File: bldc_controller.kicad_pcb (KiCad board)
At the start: 4 copper layers, 99.1 x 99.1 mm, 151 parts, among them J1 Conn_01x06_Male, J2 Screw_Terminal_01x04, Q1 2N7002E, Q10 IRLB8721PBF, Q11 IRLB8721PBF, Q2 DMN65D8L-7, Q3 DMN65D8L-7, Q4 MMBT3904, Q5 IRF4905, Q6 IRLB8721PBF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

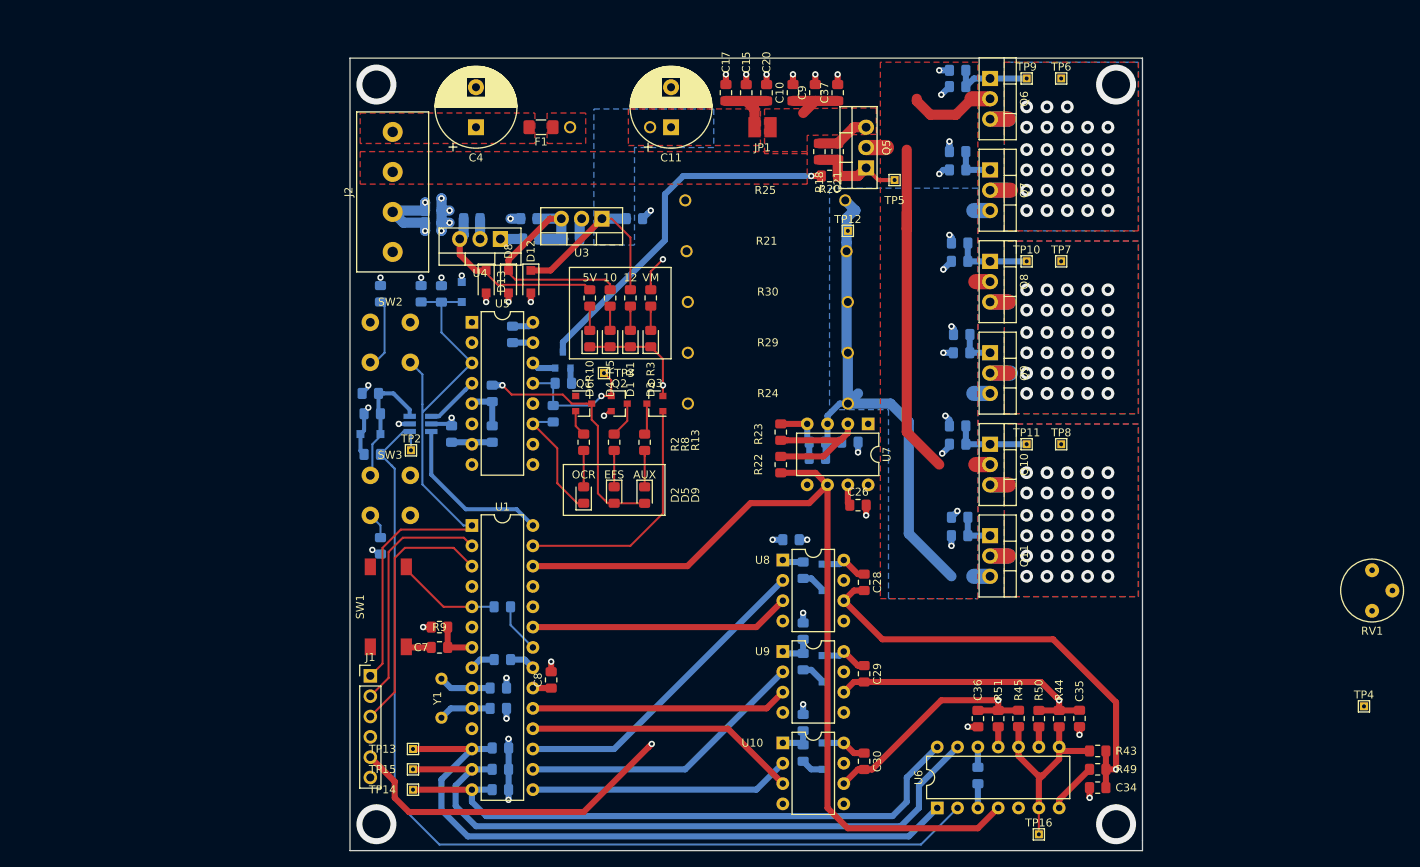
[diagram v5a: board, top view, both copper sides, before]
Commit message: Just Need to Fix Silkscreen
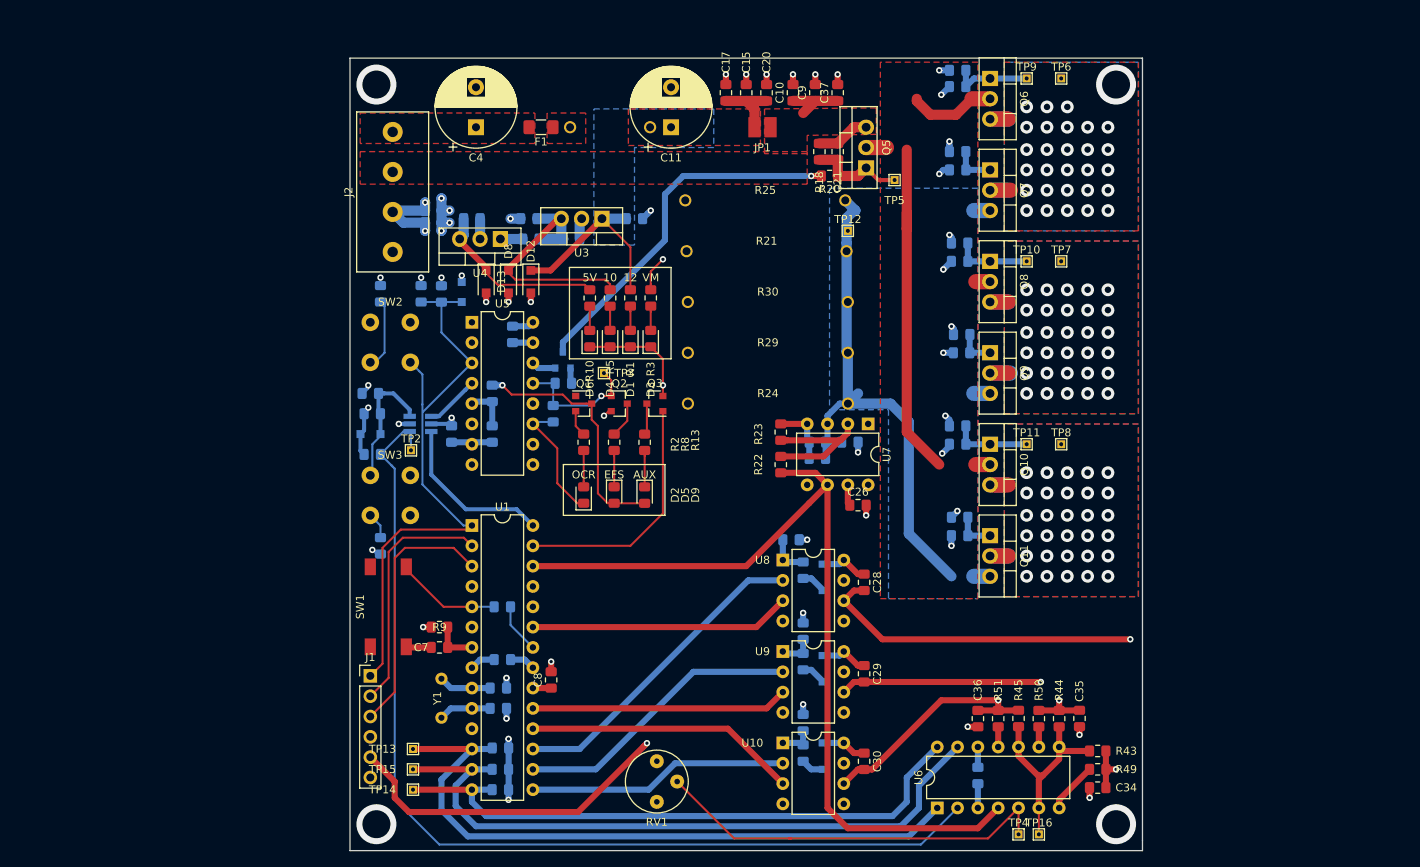
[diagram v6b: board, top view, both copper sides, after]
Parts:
- moved RV1 92.5 mm to (138.7, 129.8)
- moved TP4 46.0 mm to (183.9, 138.9)
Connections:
- RV1 pad 1: +5V -> GNDD
- RV1 pad 3: GNDD -> +5V
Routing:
- net Net-(RV1-Pad2): track 0.00 -> 50.8 mm
- net PhaseA: track 138.0 -> 128.1 mm, vias 29 -> 30
- net PhaseB: track 85.9 -> 82.7 mm, vias 31 -> 32
- net +5V: track 92.5 -> 91.8 mm
- net +12V: track 34.5 -> 33.8 mm
- net +10V: track 88.5 -> 88.6 mm, vias 2 -> 1

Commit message: Just Need to Fix Bottom Silkscreen
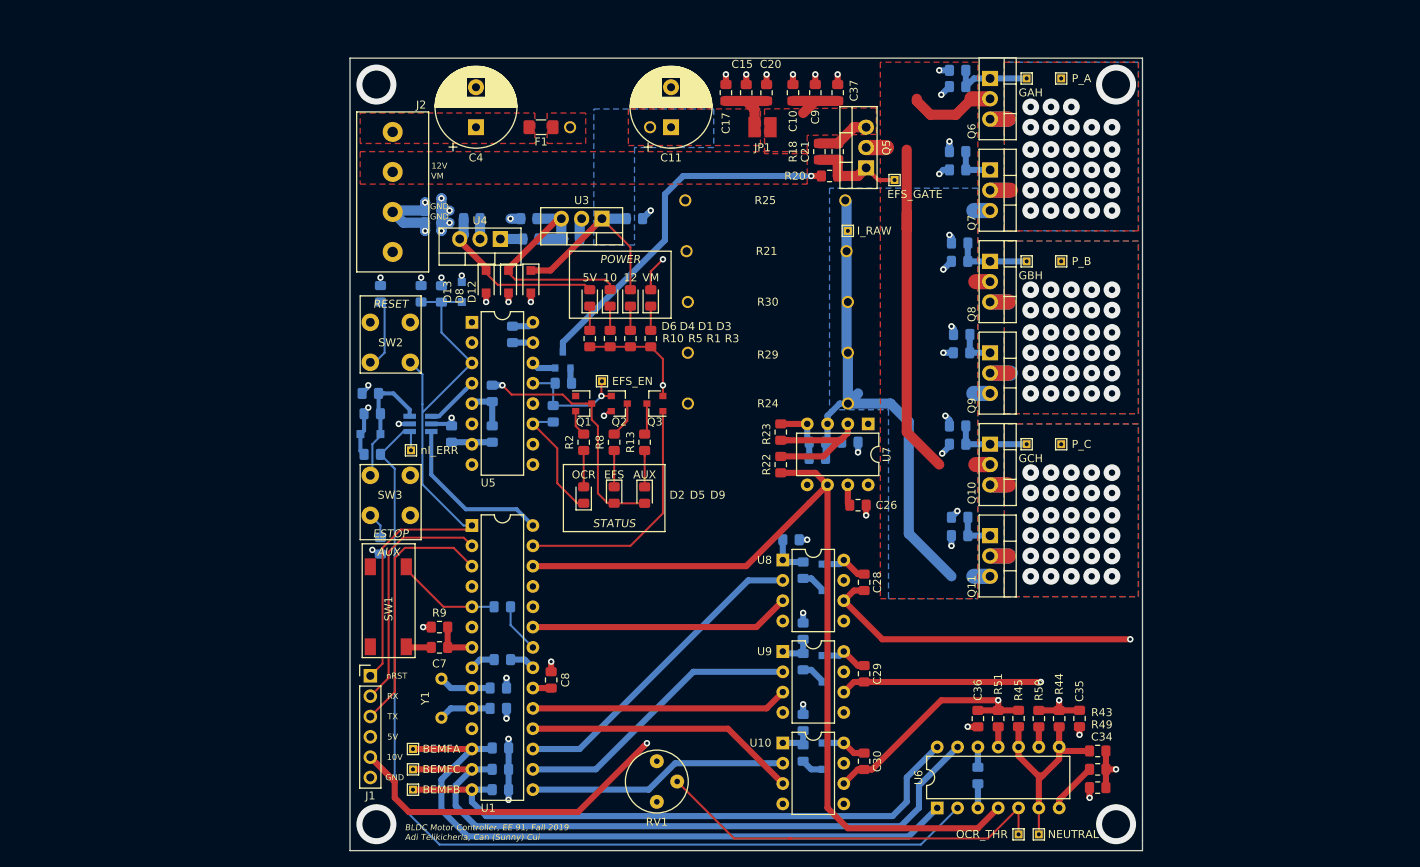
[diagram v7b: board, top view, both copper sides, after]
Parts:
- moved D6 5.09 mm to (130.3, 71.9)
- moved D1 5.08 mm to (135.4, 71.9)
- moved D3 5.08 mm to (137.9, 71.9)
- moved D4 5.08 mm to (132.8, 71.9)
- moved R1 5.08 mm to (135.4, 77.0)
- moved R3 5.08 mm to (137.9, 77.0)
- moved R10 5.07 mm to (130.3, 77.0)
- moved R5 5.07 mm to (132.8, 77.0)
- moved TP3 1.05 mm to (131.8, 82.3)
- renumbered TP12 to TP1
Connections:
- D1 pad 1: GNDD -> Net-(D1-Pad1)
- D1 pad 2: Net-(D1-Pad2) -> +12V
- D3 pad 1: GNDD -> Net-(D3-Pad1)
- D3 pad 2: Net-(D3-Pad2) -> VBUS
- D4 pad 1: GNDD -> Net-(D4-Pad1)
- D4 pad 2: Net-(D4-Pad2) -> +10V
- D6 pad 1: GNDD -> Net-(D6-Pad1)
- D6 pad 2: Net-(D6-Pad2) -> +5V
- R1 pad 1: +12V -> Net-(D1-Pad1)
- R1 pad 2: Net-(D1-Pad2) -> GNDD
- R10 pad 1: +5V -> Net-(D6-Pad1)
- R10 pad 2: Net-(D6-Pad2) -> GNDD
- R3 pad 1: VBUS -> Net-(D3-Pad1)
- R3 pad 2: Net-(D3-Pad2) -> GNDD
- R5 pad 1: +10V -> Net-(D4-Pad1)
- R5 pad 2: Net-(D4-Pad2) -> GNDD
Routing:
- net Net-(D6-Pad2): track 3.03 -> 0.00 mm
- net Net-(D6-Pad1): track 0.00 -> 3.03 mm
- net Net-(D3-Pad2): track 3.03 -> 0.00 mm
- net Net-(D3-Pad1): track 0.00 -> 3.03 mm
- net Net-(D1-Pad2): track 3.03 -> 0.00 mm
- net Net-(D1-Pad1): track 0.00 -> 3.03 mm
- net Net-(D4-Pad2): track 3.02 -> 0.00 mm
- net Net-(D4-Pad1): track 0.00 -> 3.02 mm
- net /EFUSE_EN: track 16.7 -> 15.3 mm
- net /I_RAW: track 75.1 -> 74.1 mm
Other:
- board text added: "10V"
- board text added: "12V"
- board text added: "BEMFA"
- board text added: "BEMFB"
- board text added: "BEMFC"
- board text added: "BLDC Motor Controller, EE 91, Fall 2019 Adi Telikicherla, Can (Sunny) Cui"
- board text added: "EFS_EN"
- board text added: "EFS_GATE"
- board text added: "ESTOP"
- board text added: "GAH"
- board text added: "GBH"
- board text added: "GCH"
- board text added: "GND"
- board text added: "I_RAW"
- board text added: "NEUTRAL"
- board text added: "OCR_THR"
- board text added: "POWER"
- board text added: "P_A"
- board text added: "P_B"
- board text added: "P_C"
- board text added: "RESET"
- board text added: "RX"
- board text added: "STATUS"
- board text added: "TX"
- board text added: "nI_ERR"
- board text added: "nRST"
